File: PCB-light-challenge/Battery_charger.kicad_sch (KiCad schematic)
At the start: 3 parts

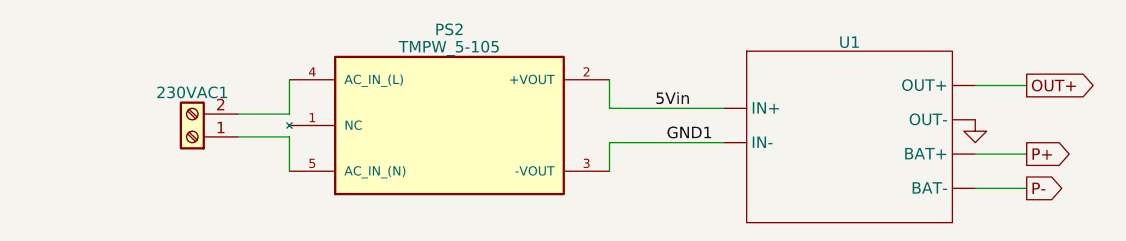
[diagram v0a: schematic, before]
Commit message: Traco footprint toegevoegd
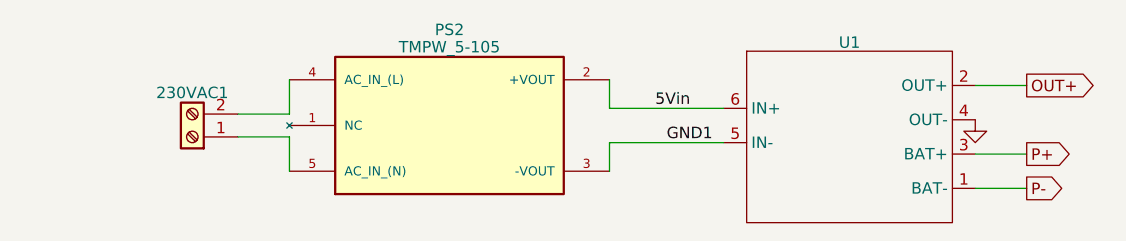
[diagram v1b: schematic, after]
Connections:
- net 5Vin: now also U1.6 (IN+); no longer U1. (OUT-)
- net GND: now also U1.4 (OUT-); no longer U1. (OUT-)
- net GND1: now also U1.5 (IN-); no longer U1. (OUT-)
- net OUT+: now also U1.2 (OUT+); no longer U1. (OUT-)
- net P+: now also U1.3 (BAT+); no longer U1. (OUT-)
- net P-: now also U1.1 (BAT-); no longer U1. (OUT-)
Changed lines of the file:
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@@
       (effects (font (size 1.27 1.27)) hide)
     )
-    (pin "")
-    (pin "")
-    (pin "")
-    (pin "")
-    (pin "")
-    (pin "")
+    (pin "3")
+    (pin "1")
+    (pin "6")
+    (pin "5")
+    (pin "2")
+    (pin "4")
     (instances
       (project "PCB-light-challenge"

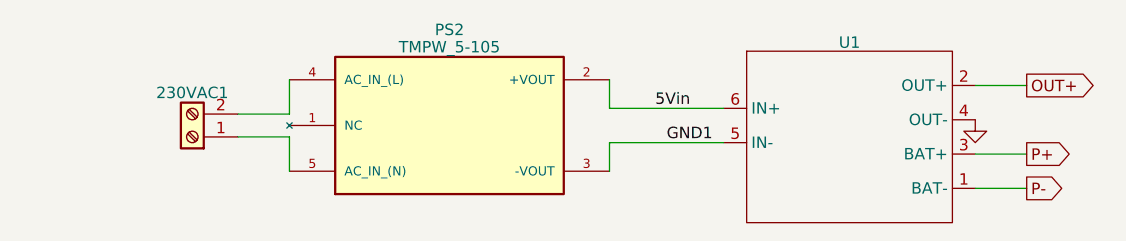
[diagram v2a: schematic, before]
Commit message: main board aangepast en ground toegevoegd
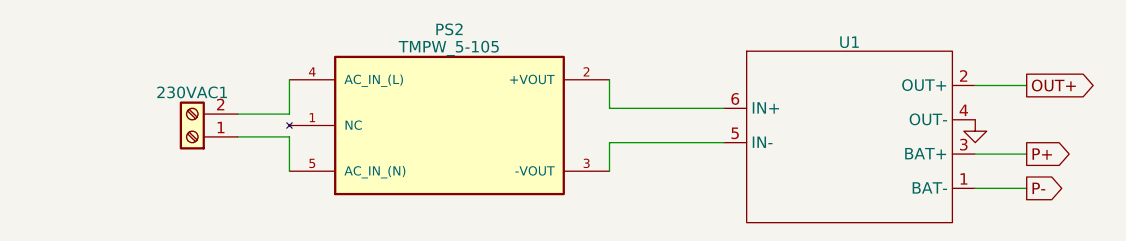
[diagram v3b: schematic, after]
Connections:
- net 5Vin: no longer names the net of PS2.2 (+VOUT), U1.6 (IN+)
- net GND1: no longer names the net of PS2.3 (-VOUT), U1.5 (IN-)
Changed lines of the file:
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@@
     (stroke (width 0) (type default))
-  )
-  (label "GND1" (at 103.505 60.96 0) (fields_autoplaced)
-    (effects (font (size 1.27 1.27)) (justify left bottom))
-  )
-  (label "5Vin" (at 102.235 57.15 0) (fields_autoplaced)
-    (effects (font (size 1.27 1.27)) (justify left bottom))
   )
   (global_label "P+" (shape output) (at 143.51 62.23 0) (fields_autoplaced)

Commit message: EDS protection en fuse toegevoegd
we moeten nog wel footprints checken
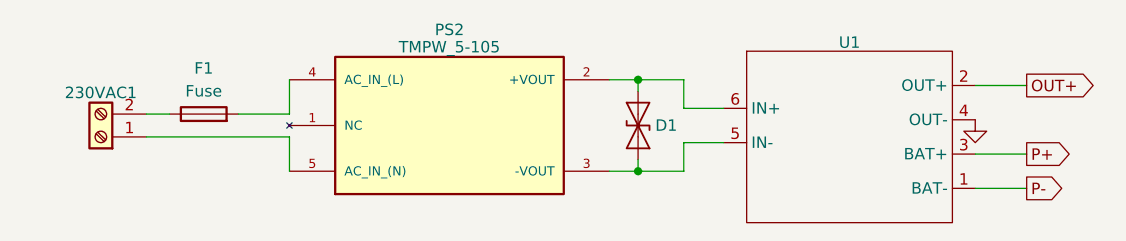
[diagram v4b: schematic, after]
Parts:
- added D1: ESD9B3.3ST5G, Diode_SMD:D_SOD-323_HandSoldering, symbol Diode:ESD9B3.3ST5G
- added F1: Fuse, symbol Device:Fuse
- 230VAC1: footprint (none) -> TerminalBlock_4Ucon:TerminalBlock_4Ucon_1x02_P3.50mm_Vertical
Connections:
- net at 230VAC1.2 (Pin_2): now also F1.1; no longer PS2.4 (AC_IN_(L))
- net at PS2.3 (-VOUT), U1.5 (IN-): now also D1.1 (A1)
- net at PS2.2 (+VOUT), U1.6 (IN+): now also D1.2 (A2)
- new net: F1.2, PS2.4 (AC_IN_(L))
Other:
- moved on the sheet: 230VAC1
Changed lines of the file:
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@@
     (company "HHS Living Labs")
+  )
+  (junction (at 100.33 64.135) (diameter 0) (color 0 0 0 0)
+  )
+  (junction (at 100.33 53.975) (diameter 0) (color 0 0 0 0)
   )
   (wire (pts (xy 137.795 62.23) (xy 143.51 62.23))
     (stroke (width 0) (type default))
   )
-  (wire (pts (xy 55.88 60.325) (xy 61.595 60.325))
+  (wire (pts (xy 109.855 57.15) (xy 105.41 57.15))
+    (stroke (width 0) (type default))
+  )
+  (wire (pts (xy 105.41 60.96) (xy 105.41 64.135))
+    (stroke (width 0) (type default))
+  )
+  (wire (pts (xy 100.33 53.975) (xy 100.33 55.245))
+    (stroke (width 0) (type default))
+  )
+  (wire (pts (xy 45.72 60.325) (xy 61.595 60.325))
     (stroke (width 0) (type default))
   )
@@
     (stroke (width 0) (type default))
   )
-  (wire (pts (xy 97.155 60.96) (xy 97.155 64.135))
+  (wire (pts (xy 105.41 53.975) (xy 105.41 57.15))
     (stroke (width 0) (type default))
   )
-  (wire (pts (xy 97.155 53.975) (xy 97.155 57.15))
+  (wire (pts (xy 45.72 57.785) (xy 48.26 57.785))
+    (stroke (width 0) (type default))
+  )
+  (wire (pts (xy 97.155 64.135) (xy 100.33 64.135))
+    (stroke (width 0) (type default))
+  )
+  (wire (pts (xy 100.33 62.865) (xy 100.33 64.135))
     (stroke (width 0) (type default))
   )
@@
     (stroke (width 0) (type default))
   )
-  (wire (pts (xy 97.155 57.15) (xy 109.855 57.15))
+  (wire (pts (xy 100.33 64.135) (xy 105.41 64.135))
     (stroke (width 0) (type default))
   )
-  (wire (pts (xy 97.155 60.96) (xy 109.855 60.96))
+  (wire (pts (xy 97.155 53.975) (xy 100.33 53.975))
+    (stroke (width 0) (type default))
+  )
+  (wire (pts (xy 109.855 60.96) (xy 105.41 60.96))
     (stroke (width 0) (type default))
   )
@@
   )
   (wire (pts (xy 137.795 66.04) (xy 143.51 66.04))
+    (stroke (width 0) (type default))
+  )
+  (wire (pts (xy 100.33 53.975) (xy 105.41 53.975))
     (stroke (width 0) (type default))
   )
@@
     )
   )
-  (symbol (lib_id "Connector:Screw_Terminal_01x02") (at 50.8 60.325 180) (unit 1)
+  (symbol (lib_id "Diode:ESD9B3.3ST5G") (at 100.33 59.055 90) (unit 1)
+    (in_bom yes) (on_board yes) (dnp no)
+    (property "Reference" "D1" (at 102.235 59.055 90)
+      (effects (font (size 1.27 1.27)) (justify right))
+    )
+    (property "Value" "ESD9B3.3ST5G" (at 103.505 60.325 90)
+      (effects (font (size 1.27 1.27)) (justify right) hide)
+    )
+    (property "Footprint" "Diode_SMD:D_SOD-323_HandSoldering" (at 100.33 59.055 0)
+      (effects (font (size 1.27 1.27)) hide)
+    )
+    (property "Datasheet" "https://www.onsemi.com/pub/Collateral/ESD9B-D.PDF" (at 100.33 59.055 0)
+      (effects (font (size 1.27 1.27)) hide)
+    )
+    (pin "1")
+    (pin "2")
+    (instances
+      (project "PCB-light-challenge"
+        (path "/35573e8f-7834-430c-81d2-239f316c7834/1ee2b17a-9b36-4608-9d61-b871128bc979"
+          (reference "D1") (unit 1)
+        )
+      )
+    )
+  )
+  (symbol (lib_id "Connector:Screw_Terminal_01x02") (at 40.64 60.325 180) (unit 1)
     (in_bom yes) (on_board yes) (dnp no) (fields_autoplaced)
-    (property "Reference" "230VAC1" (at 50.8 55.4261 0)
+    (property "Reference" "230VAC1" (at 40.64 55.4261 0)
       (effects (font (size 1.27 1.27)))
     )
-    (property "Value" "Screw_Terminal_01x02" (at 50.8 55.4261 0)
+    (property "Value" "Screw_Terminal_01x02" (at 40.64 55.4261 0)
       (effects (font (size 1.27 1.27)) hide)
     )
-    (property "Footprint" "" (at 50.8 60.325 0)
+    (property "Footprint" "TerminalBlock_4Ucon:TerminalBlock_4Ucon_1x02_P3.50mm_Vertical" (at 40.64 60.325 0)
       (effects (font (size 1.27 1.27)) hide)
     )
-    (property "Datasheet" "~" (at 50.8 60.325 0)
+    (property "Datasheet" "~" (at 40.64 60.325 0)
       (effects (font (size 1.27 1.27)) hide)
     )
@@
         )
       )
+    )
+  )
+  (symbol (lib_id "Device:Fuse") (at 52.07 57.785 90) (unit 1)
+    (in_bom yes) (on_board yes) (dnp no) (fields_autoplaced)
+    (property "Reference" "F1" (at 52.07 52.705 90)
+      (effects (font (size 1.27 1.27)))
+    )
+    (property "Value" "Fuse" (at 52.07 55.245 90)
+      (effects (font (size 1.27 1.27)))
+    )
+    (property "Footprint" "" (at 52.07 59.563 90)
+      (effects (font (size 1.27 1.27)) hide)
+    )
+    (property "Datasheet" "~" (at 52.07 57.785 0)
+      (effects (font (size 1.27 1.27)) hide)
+    )
+    (pin "1")
+    (pin "2")
+    (instances
+      (project "PCB-light-challenge"
+        (path "/35573e8f-7834-430c-81d2-239f316c7834/1ee2b17a-9b36-4608-9d61-b871128bc979"
+          (reference "F1") (unit 1)
+        )
+      )

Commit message: PCB 80% af
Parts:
- removed PS2: TMPW_5-105, TMPW_5-105:CONV_TMPW_5-105, symbol TMPW_5-105:TMPW_5-105
- added PS1: TMPS_05-105, KiCad:TMPS05-105, symbol TMPS_05-105:TMPS_05-105
- 230VAC1: footprint TerminalBlock_4Ucon:TerminalBlock_4Ucon_1x02_P3.50mm_Vertical -> TerminalBlock_TE-Connectivity:TerminalBlock_TE_282834-2_1x02_P2.54mm_Horizontal
- F1: footprint (none) -> 3557-2:FUSE_3557-2
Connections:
- net P- is gone; now on net GND: U1.1 (BAT-)
- net at D1.1 (A1), U1.5 (IN-): now also PS1.4 (-VOUT)
- net +5V: now reaches D1.2 (A2), U1.6 (IN+)
- net +5V: now also PS1.5 (+VOUT)
- net GNDAC: now reaches 230VAC1.1 (Pin_1)
- net GNDAC: now also PS1.2 (AC(L))
- net Fuse_in: now reaches 230VAC1.2 (Pin_2)
- net Fuse_in: now also F1.2_1, F1.2_2; no longer F1.1
- new net Fuse: F1.1_1, F1.1_2, PS1.1 (AC(N))
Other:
- moved on the sheet: 230VAC1
